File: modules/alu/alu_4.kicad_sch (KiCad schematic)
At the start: 60 parts, among them Q457 2N3906, Q458 2N3906, Q459 2N3906, Q460 2N3906, Q461 2N3906, Q462 2N3906, Q463 2N3906, Q464 2N3906, Q465 2N3904, Q466 2N3904, Q467 2N3904, Q468 2N3904, Q469 2N3904, Q470 2N3904, Q471 2N3904, Q472 2N3904, Q473 2N3904, Q474 2N3904, Q475 2N3904, Q476 2N3904, Q477 2N3904, Q478 2N3904, Q479 2N3904, Q480 2N3904, Q481 2N3906, Q482 2N3906, Q483 2N3906, Q484 2N3906

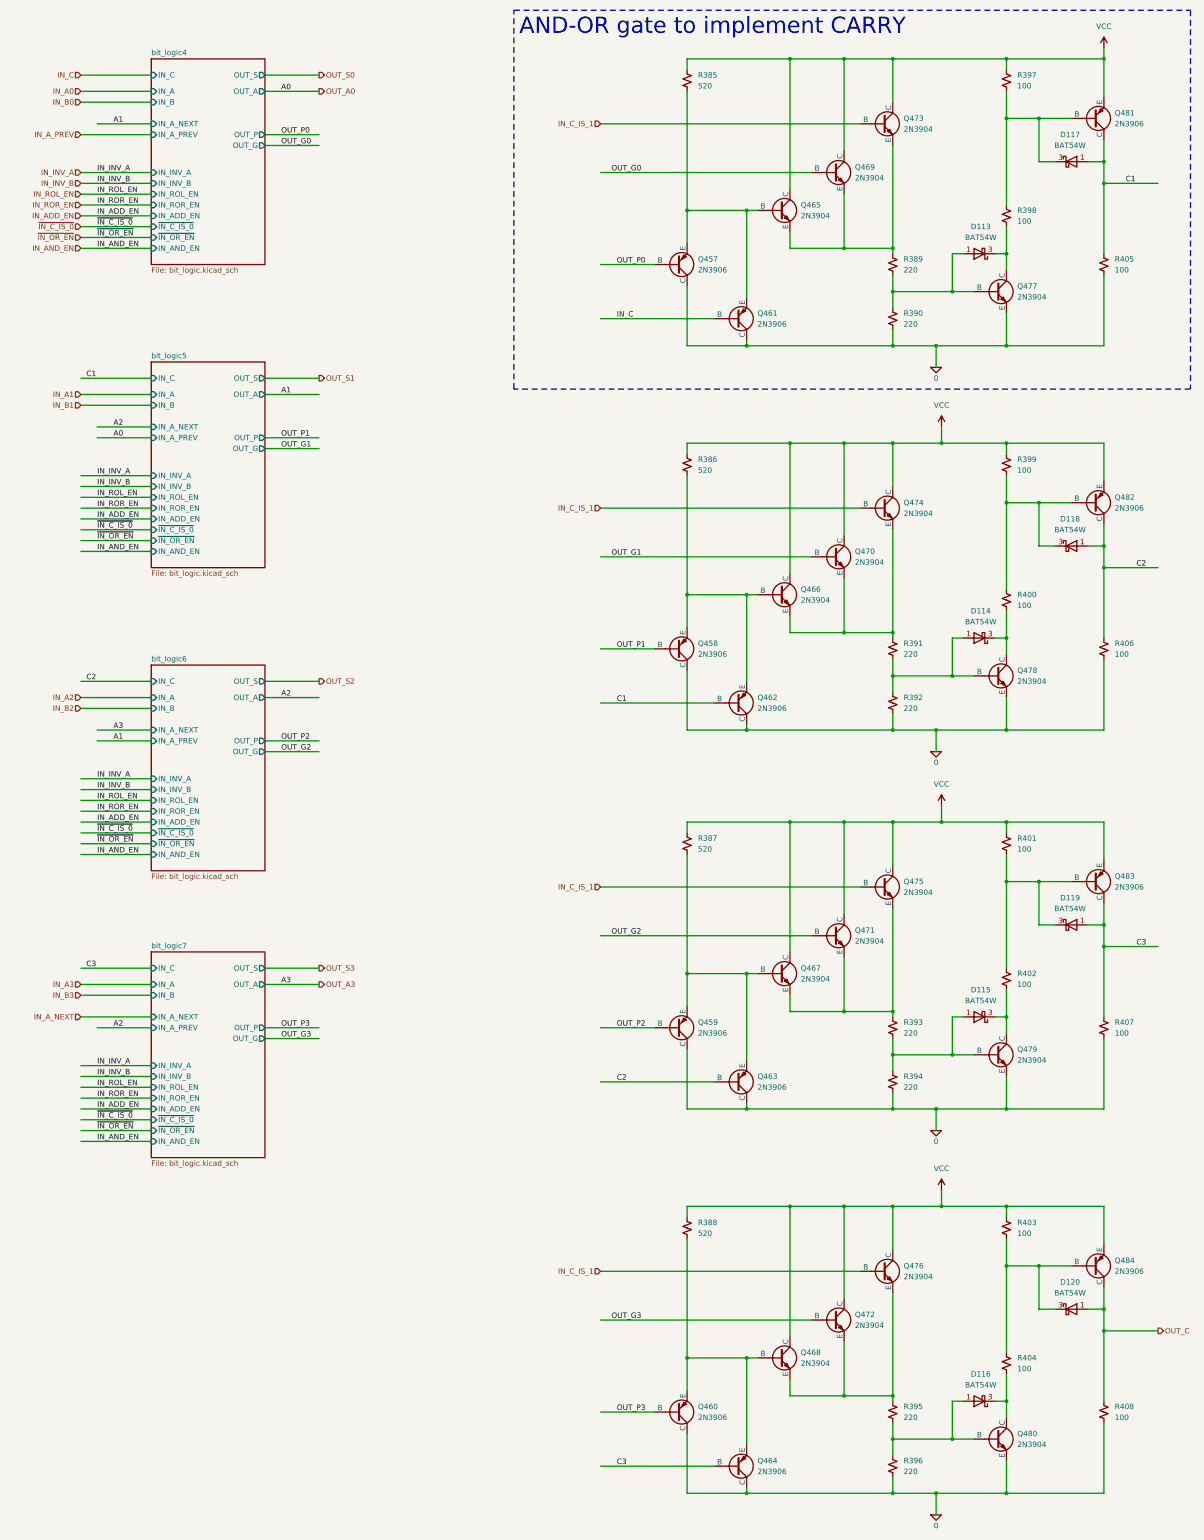
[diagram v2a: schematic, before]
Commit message: Moved carry generation into ALU bit-cell.
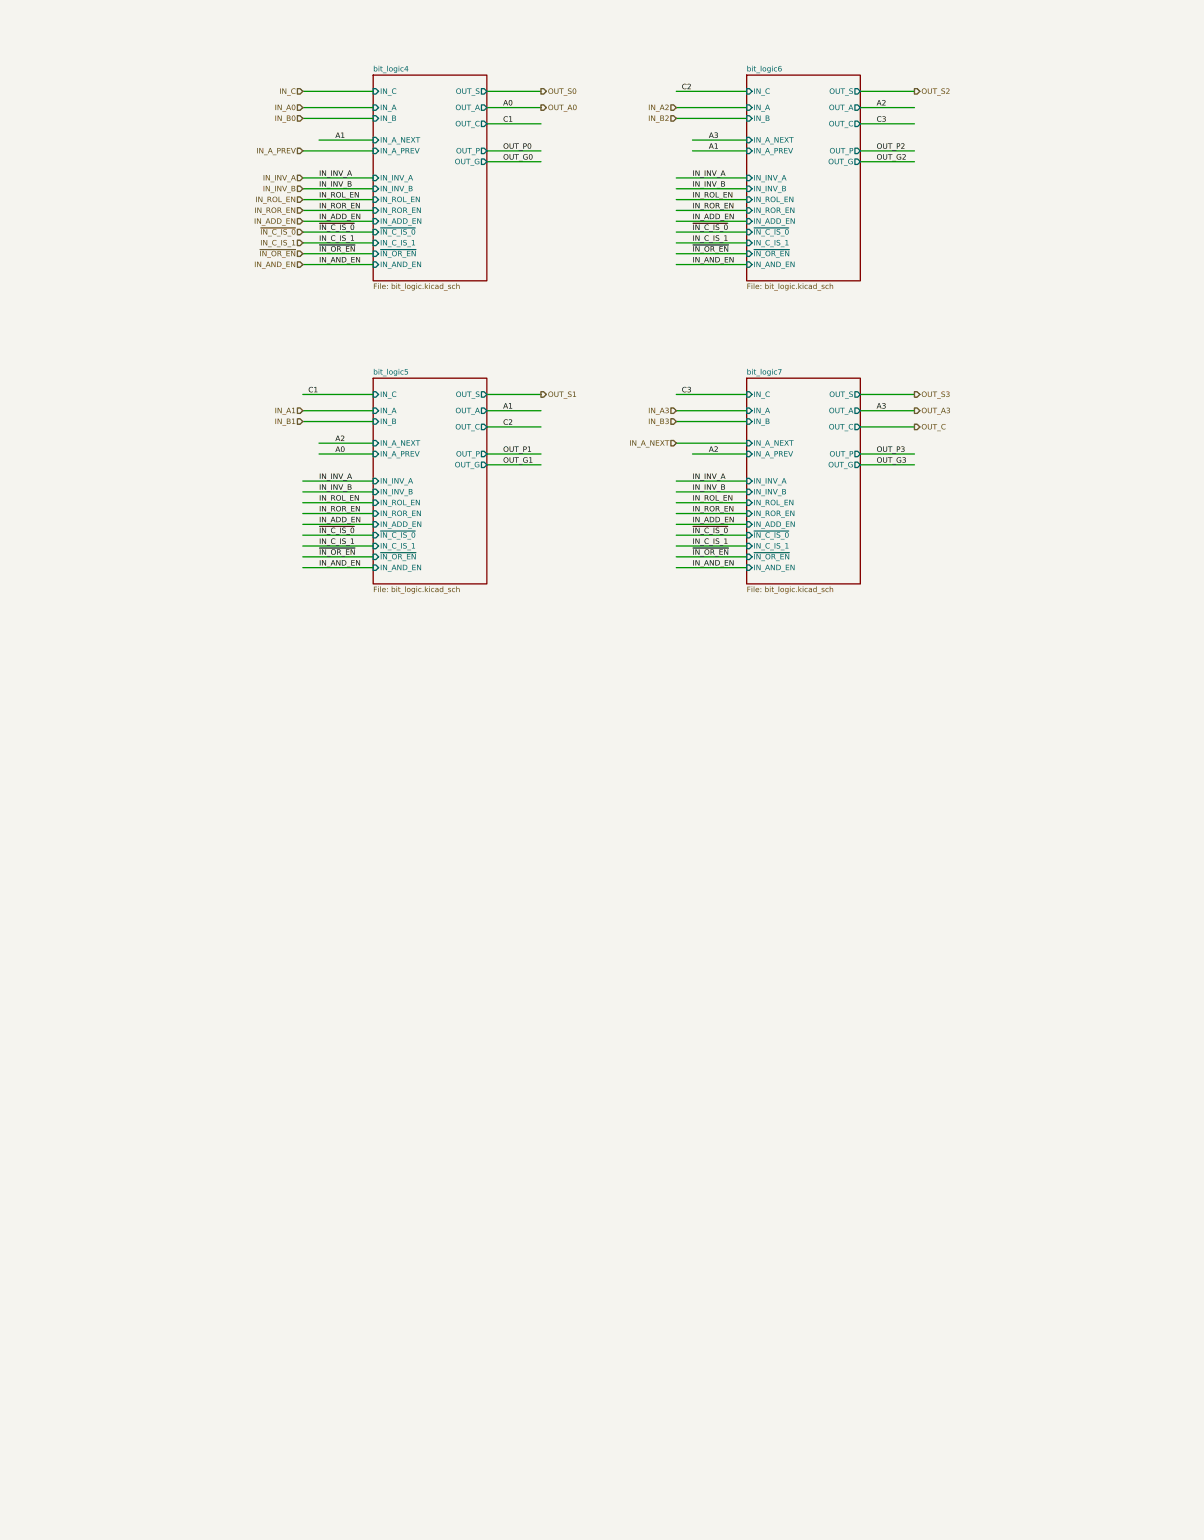
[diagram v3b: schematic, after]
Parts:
- removed D113, D114, D115, D116, D117, D118, D119, D120: BAT54W, Package_TO_SOT_SMD:SOT-323_SC-70, symbol Diode:BAT54W
- removed Q457, Q458, Q459, Q460, Q461, Q462, Q463, Q464, Q481, Q482, Q483, Q484: 2N3906, Package_TO_SOT_SMD:SOT-23-3, symbol Simulation_SPICE:PNP
- removed Q465, Q466, Q467, Q468, Q469, Q470, Q471, Q472, Q473, Q474, Q475, Q476, Q477, Q478, Q479, Q480: 2N3904, Package_TO_SOT_SMD:SOT-23-3, symbol Simulation_SPICE:NPN
- removed R385, R386, R387, R388: 520, Resistor_SMD:R_0603_1608Metric_Pad0.98x0.95mm_HandSolder, symbol Device:R_Small_US
- removed R389, R390, R391, R392, R393, R394, R395, R396: 220, Resistor_SMD:R_0603_1608Metric_Pad0.98x0.95mm_HandSolder, symbol Device:R_Small_US
- removed R397, R398, R399, R400, R401, R402, R403, R404, R405, R406, R407, R408: 100, Resistor_SMD:R_0603_1608Metric_Pad0.98x0.95mm_HandSolder, symbol Device:R_Small_US
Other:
- sheet bit_logic4 ports: added IN_C_IS_1, OUT_C; removed none
- sheet bit_logic5 ports: added IN_C_IS_1, OUT_C; removed none
- sheet bit_logic6 ports: added IN_C_IS_1, OUT_C; removed none
- sheet bit_logic7 ports: added IN_C_IS_1, OUT_C; removed none
- note removed: "AND-OR gate to implement CARRY"
